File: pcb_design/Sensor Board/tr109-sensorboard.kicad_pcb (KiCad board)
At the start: 2 copper layers, 65 x 30 mm, 57 parts, among them J1 Conn_01x01_Female, J2 Conn_01x01_Female, J47 Raspberry_Pi_2_3, U1 BME680, U2 74HC595, U3 AMG8833, U4 LIS3MDLTR

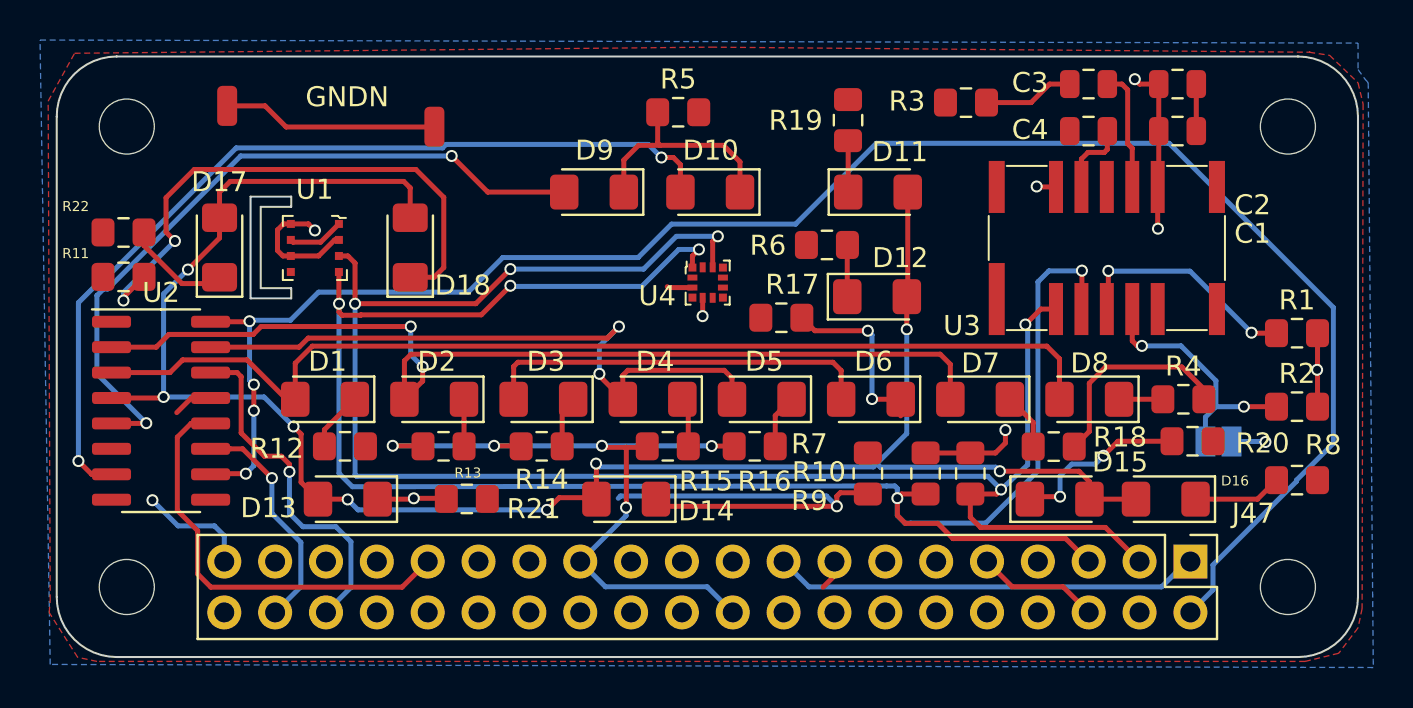
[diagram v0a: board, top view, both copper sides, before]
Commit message: cleanup and revisions
changes to the sensor and main boards
clean up of the blender file to remove some deprecated meshes
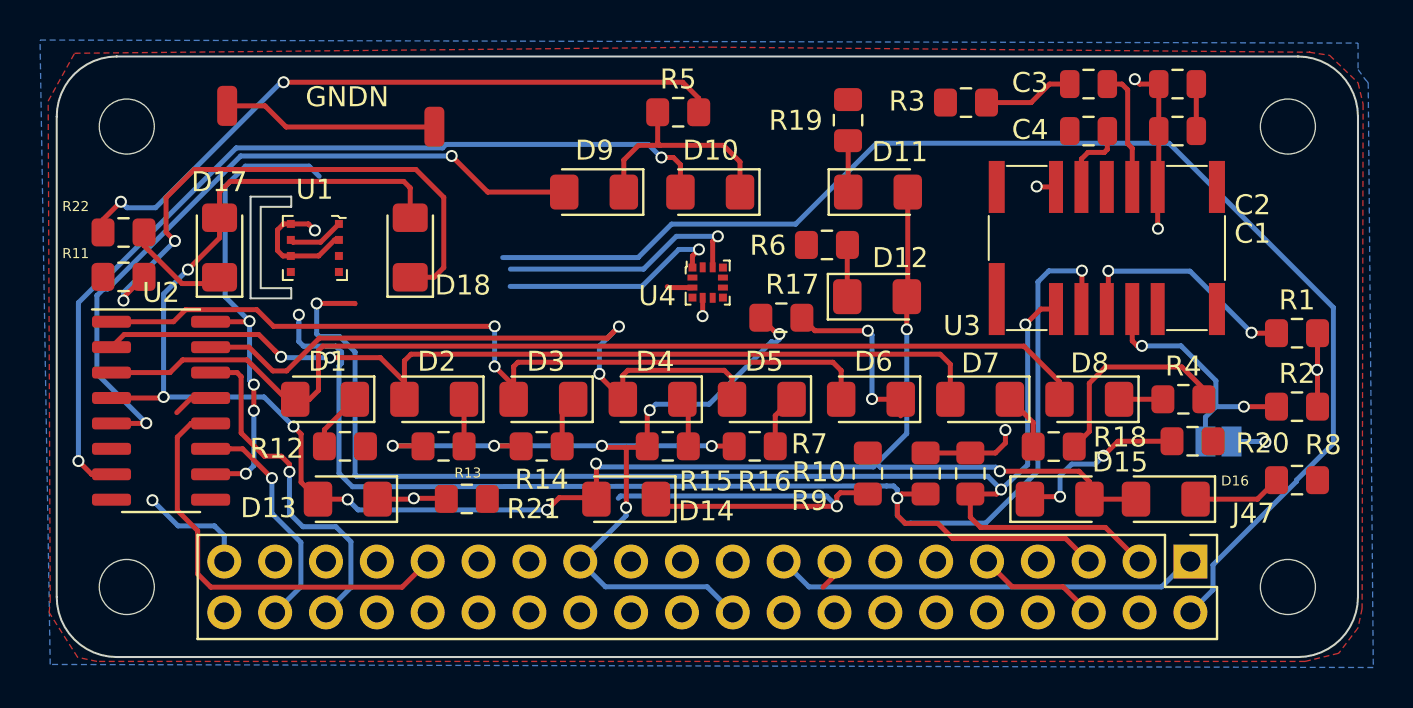
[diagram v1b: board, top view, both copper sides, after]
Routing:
- net GND: track 70.0 -> 116.0 mm, vias 7 -> 11
- net BETA: track 19.7 -> 43.6 mm, vias 0 -> 2
- net SCK: track 95.5 -> 85.5 mm, vias 5 -> 4
- net SDA: track 88.9 -> 80.8 mm, vias 5 -> 4
- net DELTA: track 50.9 -> 48.0 mm
- net 5V: track 91.1 -> 89.7 mm
- net ALPHA: track 33.3 -> 34.3 mm
- net GAMMA: track 52.9 -> 52.3 mm

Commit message: sensor board revisions
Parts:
- removed G***: LOGO, logo:delta 3
- removed U4: LIS3MDLTR, digikey-footprints:VFLGA-12_2x2mm
- added J3: Conn_01x04_Female, Connector_PinHeader_2.54mm:PinHeader_1x04_P2.54mm_Vertical, F.Cu at (129.3, 105.9)
- J1, J2: footprint Connector_Wire:SolderWirePad_1x01_SMD_1x2mm -> TestPoint:TestPoint_Pad_1.0x1.0mm
- moved R10 22.2 mm to (162.4, 103.9), turned to 0 degrees
- moved R9 19.1 mm to (162.4, 106.2), turned to 0 degrees
- moved R17 7.49 mm to (137.5, 101.0), turned to 90 degrees
- moved R6 1.69 mm to (140.7, 104.9), turned to 0 degrees
- moved J2 1.60 mm to (118.4, 97.7)
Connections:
- U1 pad 5: Net-(U1-Pad5) -> GND
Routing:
- net SCK: track 85.5 -> 109.6 mm, vias 4 -> 3
- net SDA: track 80.8 -> 99.7 mm, vias 4 -> 6
- net GND: track 116.0 -> 132.0 mm, vias 11 -> 16
- net 3.3V: track 46.4 -> 55.4 mm
- net Net-(D6-Pad1): track 9.33 -> 15.9 mm
- net 5V: track 89.7 -> 87.4 mm, vias 4 -> 6
- net Net-(J1-Pad1): track 10.8 -> 9.36 mm
- net ANIM2: track 45.0 -> 46.1 mm, vias 2 -> 4
- net ANIM1: track 36.1 -> 36.6 mm
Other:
- outline, holes or cut-outs redrawn
- board text added: "3v3"
- board text added: "EXT SENSOR"
- board text added: "GND"
- board text added: "SCK"
- board text added: "SDA"
